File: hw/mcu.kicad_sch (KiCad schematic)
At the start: 20 parts, among them J2 Conn_01x06_Socket, J3 Conn_01x01_Socket, Q1 IRLML6244, Q2 IRLML6244, SW4 RST, SW5 BOOT, U4 ESP32-WROOM-E

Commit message: Version 1.1 changes
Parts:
- removed NT3: NetTie_2, NetTie_Vasil:NetTie-2_SMD_Pad0.20mm, symbol Device:NetTie_2
- removed SW4: RST, Button_Switch_SMD:SW_Push_SPST_NO_Alps_SKRK, symbol Switch:SW_Push
- removed SW5: BOOT, Button_Switch_SMD:SW_SPDT_PCM12, symbol Switch:SW_Push
- added C14: 100n, Capacitor_SMD:C_0805_2012Metric_Pad1.18x1.45mm_HandSolder, symbol Device:C_Small
- added D1: LED_Small, LED_SMD:LED_0805_2012Metric_Pad1.15x1.40mm_HandSolder, symbol Device:LED_Small
- added R1: 470, Resistor_SMD:R_0805_2012Metric_Pad1.20x1.40mm_HandSolder, symbol Device:R_Small
- added R11, R12: 20k, Resistor_SMD:R_0805_2012Metric_Pad1.20x1.40mm_HandSolder, symbol Device:R_Small
- J2, J3: now fitted; now left out of the parts list
- R13: renamed from R11; value 10k -> 20k
- R14: renamed from R12; value 10k -> 20k
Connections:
- net +3V3: now also R11.1, R12.1
- net GND: now also C14.2, R1.1
- net MCU_BOOT: now also R12.2
- net MCU_EN: now also C14.1, R11.2
- net TB3: now also U4.13 (MTMS/GPIO14/ADC2_CH6)
- net LED: now reaches U4.24 (ADC2_CH2/GPIO2)
- net LED: now also D1.2 (A)
- new net: D1.1 (K), R1.2
- no-connect marks 14 -> 12
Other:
- moved on the sheet: JP1, JP2

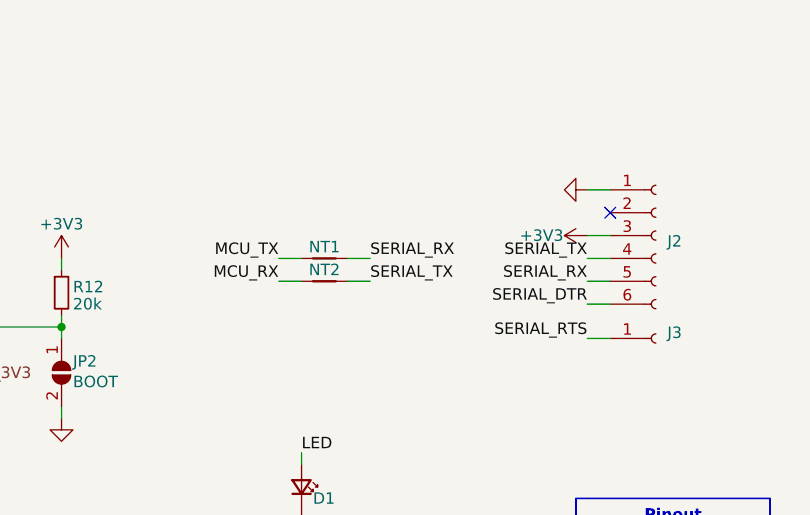
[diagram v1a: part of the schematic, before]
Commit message: Fix via annular width, remove netties
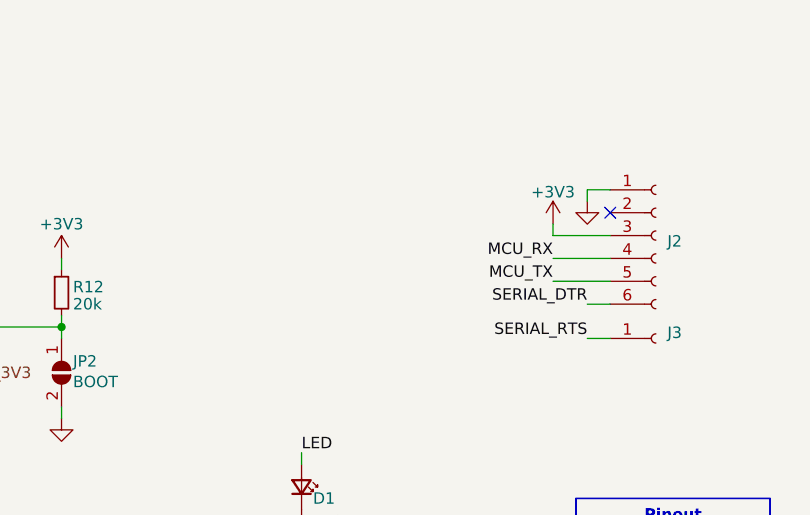
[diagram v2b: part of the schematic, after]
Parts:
- removed NT1, NT2: NetTie_2, NetTie_Vasil:NetTie-2_SMD_Pad0.20mm, symbol Device:NetTie_2
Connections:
- net SERIAL_RX is gone; now on net MCU_TX: J2.5 (Pin_5)
- net SERIAL_TX is gone; now on net MCU_RX: J2.4 (Pin_4)
